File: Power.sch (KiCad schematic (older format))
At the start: 7 parts, among them J7 Screw_Terminal_01x02

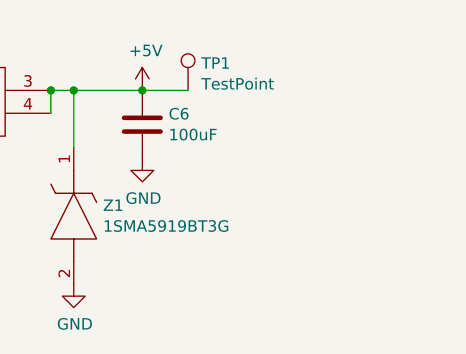
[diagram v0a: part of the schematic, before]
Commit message: Added in Servo Outputs and Setup the timers in CubeMX
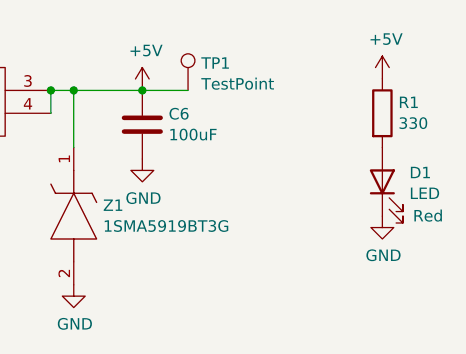
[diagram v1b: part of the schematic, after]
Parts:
- added D1: LED, LED_SMD:LED_0603_1608Metric_Pad1.05x0.95mm_HandSolder, symbol Device:LED
- added R1: 330, Resistor_SMD:R_0603_1608Metric_Pad1.05x0.95mm_HandSolder, symbol Device:R
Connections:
- net +5V: now also R1.1
- net GND: now also D1.1 (K)
- new net: D1.2 (A), R1.2
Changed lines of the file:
@@
 $Descr A4 11693 8268
 encoding utf-8
-Sheet 4 5
+Sheet 4 7
 Title "Power handling"
 Date ""
@@
 Text HLabel 3750 3100 0    50   Input ~ 0
 VDD_5V_Brick
+$Comp
+L Device:LED D?
+U 1 1 5F06186F
+P 7750 3500
+AR Path="/5F06186F" Ref="D?"  Part="1"
+AR Path="/5EF6B0D5/5F06186F" Ref="D1"  Part="1"
+F 0 "D1" V 7789 3382 50  0000 R CNN
+F 1 "LED" V 7698 3382 50  0000 R CNN
+F 2 "LED_SMD:LED_0603_1608Metric_Pad1.05x0.95mm_HandSolder" H 7750 3500 50  0001 C CNN
+F 3 "http://www.farnell.com/datasheets/2186941.pdf" H 7750 3500 50  0001 C CNN
+F 4 "SML-D15UWT86C" V 7750 3500 50  0001 C CNN "PartNumber"
+F 5 "ROHM" V 7750 3500 50  0001 C CNN "Manufacturer"
+F 6 "Red" V 7600 3300 50  0000 C CNN "Colour"
+	1    7750 3500
+	0    -1   -1   0
+$EndComp
+$Comp
+L Device:R R?
+U 1 1 5F061875
+P 7750 3200
+AR Path="/5F061875" Ref="R?"  Part="1"
+AR Path="/5EF6B0D5/5F061875" Ref="R1"  Part="1"
+F 0 "R1" H 7820 3246 50  0000 L CNN
+F 1 "330" H 7820 3155 50  0000 L CNN
+F 2 "Resistor_SMD:R_0603_1608Metric_Pad1.05x0.95mm_HandSolder" V 7680 3200 50  0001 C CNN
+F 3 "~" H 7750 3200 50  0001 C CNN
+	1    7750 3200
+	1    0    0    -1
+$EndComp
+$Comp
+L power:+5V #PWR?
+U 1 1 5F06187B
+P 7750 3050
+AR Path="/5F06187B" Ref="#PWR?"  Part="1"
+AR Path="/5EF6B0D5/5F06187B" Ref="#PWR015"  Part="1"
+F 0 "#PWR015" H 7750 2900 50  0001 C CNN
+F 1 "+5V" H 7765 3223 50  0000 C CNN
+F 2 "" H 7750 3050 50  0001 C CNN
+F 3 "" H 7750 3050 50  0001 C CNN
+	1    7750 3050
+	1    0    0    -1
+$EndComp
+$Comp
+L power:GND #PWR?
+U 1 1 5F061881
+P 7750 3650
+AR Path="/5F061881" Ref="#PWR?"  Part="1"
+AR Path="/5EF6B0D5/5F061881" Ref="#PWR016"  Part="1"
+F 0 "#PWR016" H 7750 3400 50  0001 C CNN
+F 1 "GND" H 7755 3477 50  0000 C CNN
+F 2 "" H 7750 3650 50  0001 C CNN
+F 3 "" H 7750 3650 50  0001 C CNN
+	1    7750 3650
+	1    0    0    -1
+$EndComp
 $EndSCHEMATC

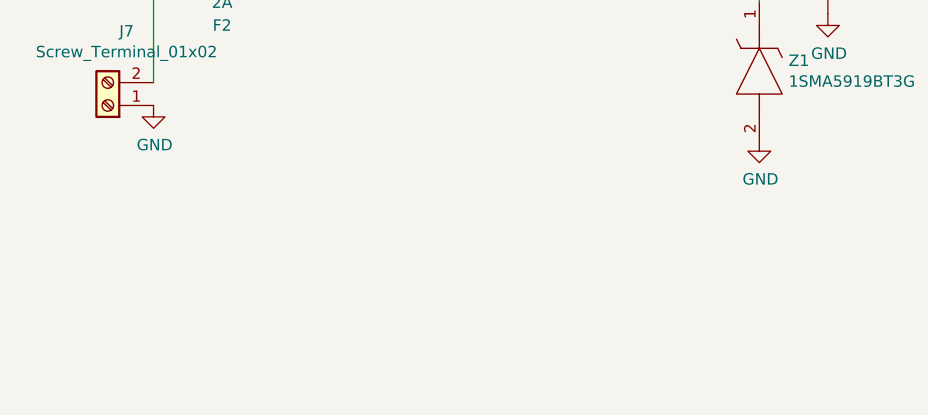
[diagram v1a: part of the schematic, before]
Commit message: Added in Buzzer and N channel mosfet
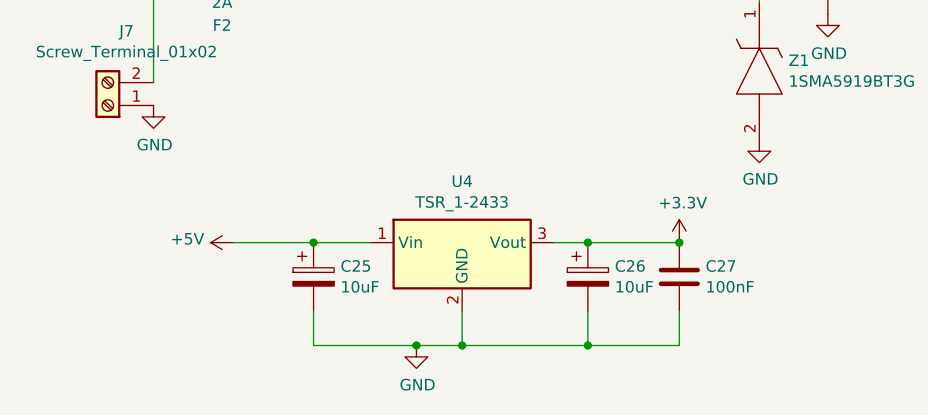
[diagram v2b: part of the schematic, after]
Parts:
- added C25, C26: 10uF, symbol Device:CP
- added C27: 100nF, symbol Device:C
- added U4: TSR_1-2433, Converter_DCDC:Converter_DCDC_TRACO_TSR-1_THT, symbol Regulator_Switching:TSR_1-2433
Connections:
- net +5V: now also C25.1, U4.1 (Vin)
- net GND: now also C25.2, C26.2, C27.2, U4.2 (GND)
- new net +3V3: C26.1, C27.1, U4.3 (Vout)
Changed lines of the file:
@@
 	1    0    0    -1
 $EndComp
+$Comp
+L Regulator_Switching:TSR_1-2433 U4
+U 1 1 5F0F90EB
+P 5100 4500
+F 0 "U4" H 5100 4867 50  0000 C CNN
+F 1 "TSR_1-2433" H 5100 4776 50  0000 C CNN
+F 2 "Converter_DCDC:Converter_DCDC_TRACO_TSR-1_THT" H 5100 4350 50  0001 L CIN
+F 3 "http://www.tracopower.com/products/tsr1.pdf" H 5100 4500 50  0001 C CNN
+	1    5100 4500
+	1    0    0    -1
+$EndComp
+$Comp
+L power:+5V #PWR027
+U 1 1 5F0FA9E4
+P 4100 4400
+F 0 "#PWR027" H 4100 4250 50  0001 C CNN
+F 1 "+5V" V 4115 4528 50  0000 L CNN
+F 2 "" H 4100 4400 50  0001 C CNN
+F 3 "" H 4100 4400 50  0001 C CNN
+	1    4100 4400
+	0    -1   -1   0
+$EndComp
+Wire Wire Line
+	4450 4700 4450 4850
+Wire Wire Line
+	4450 4850 4900 4850
+Wire Wire Line
+	5100 4850 5100 4700
+$Comp
+L power:GND #PWR028
+U 1 1 5F0FC46C
+P 4900 4850
+F 0 "#PWR028" H 4900 4600 50  0001 C CNN
+F 1 "GND" H 4905 4677 50  0000 C CNN
+F 2 "" H 4900 4850 50  0001 C CNN
+F 3 "" H 4900 4850 50  0001 C CNN
+	1    4900 4850
+	1    0    0    -1
+$EndComp
+Connection ~ 4900 4850
+Wire Wire Line
+	4900 4850 5100 4850
+Wire Wire Line
+	5650 4700 5650 4850
+Wire Wire Line
+	5650 4850 5100 4850
+Connection ~ 5100 4850
+$Comp
+L Device:C C27
+U 1 1 5F100D4B
+P 6050 4550
+F 0 "C27" H 6165 4596 50  0000 L CNN
+F 1 "100nF" H 6165 4505 50  0000 L CNN
+F 2 "" H 6088 4400 50  0001 C CNN
+F 3 "~" H 6050 4550 50  0001 C CNN
+	1    6050 4550
+	1    0    0    -1
+$EndComp
+Wire Wire Line
+	6050 4700 6050 4850
+Wire Wire Line
+	6050 4850 5650 4850
+Connection ~ 5650 4850
+Wire Wire Line
+	5500 4400 5650 4400
+$Comp
+L Device:CP C26
+U 1 1 5F102DEA
+P 5650 4550
+F 0 "C26" H 5768 4596 50  0000 L CNN
+F 1 "10uF" H 5768 4505 50  0000 L CNN
+F 2 "" H 5688 4400 50  0001 C CNN
+F 3 "~" H 5650 4550 50  0001 C CNN
+	1    5650 4550
+	1    0    0    -1
+$EndComp
+Connection ~ 5650 4400
+Wire Wire Line
+	5650 4400 6050 4400
+Wire Wire Line
+	4100 4400 4450 4400
+$Comp
+L Device:CP C25
+U 1 1 5F103B0A
+P 4450 4550
+F 0 "C25" H 4568 4596 50  0000 L CNN
+F 1 "10uF" H 4568 4505 50  0000 L CNN
+F 2 "" H 4488 4400 50  0001 C CNN
+F 3 "~" H 4450 4550 50  0001 C CNN
+	1    4450 4550
+	1    0    0    -1
+$EndComp
+Connection ~ 4450 4400
+Wire Wire Line
+	4450 4400 4700 4400
+$Comp
+L power:+3.3V #PWR029
+U 1 1 5F105C55
+P 6050 4400
+F 0 "#PWR029" H 6050 4250 50  0001 C CNN
+F 1 "+3.3V" H 6065 4573 50  0000 C CNN
+F 2 "" H 6050 4400 50  0001 C CNN
+F 3 "" H 6050 4400 50  0001 C CNN
+	1    6050 4400
+	1    0    0    -1
+$EndComp
+Connection ~ 6050 4400
 $EndSCHEMATC

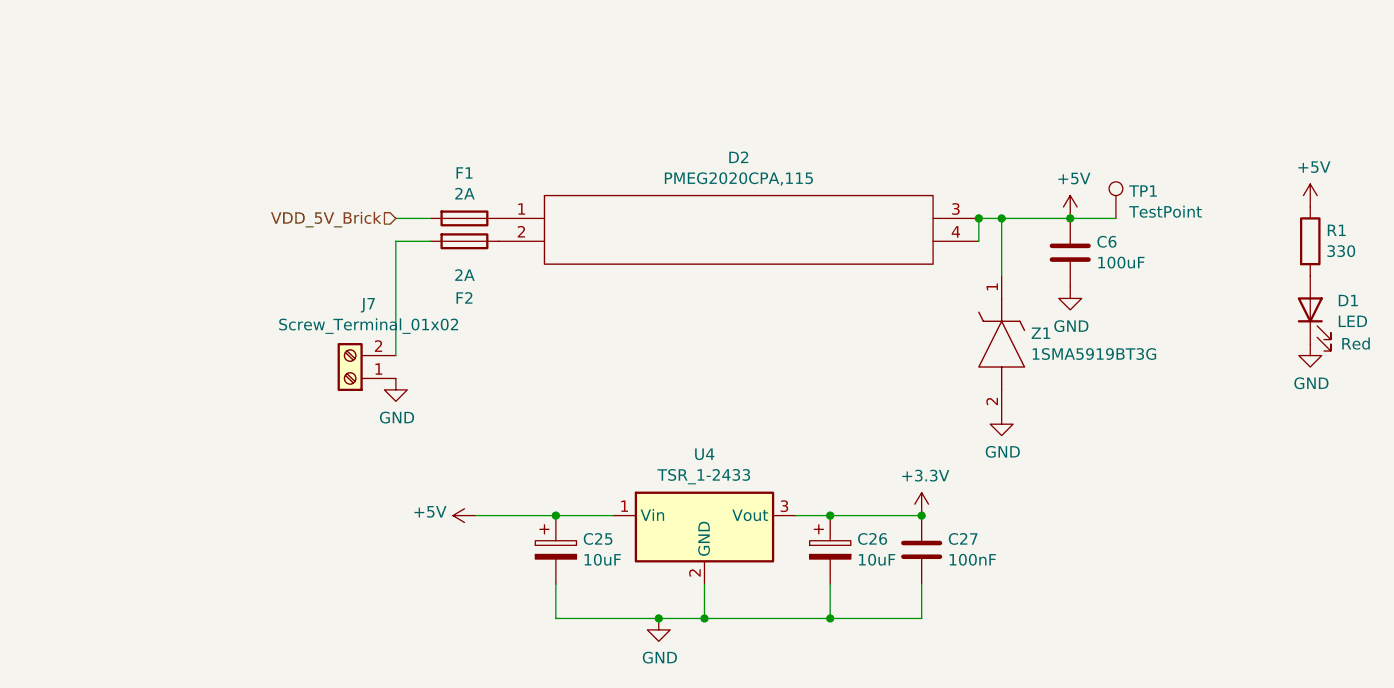
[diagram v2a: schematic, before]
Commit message: IMU1/2 added in plus regs
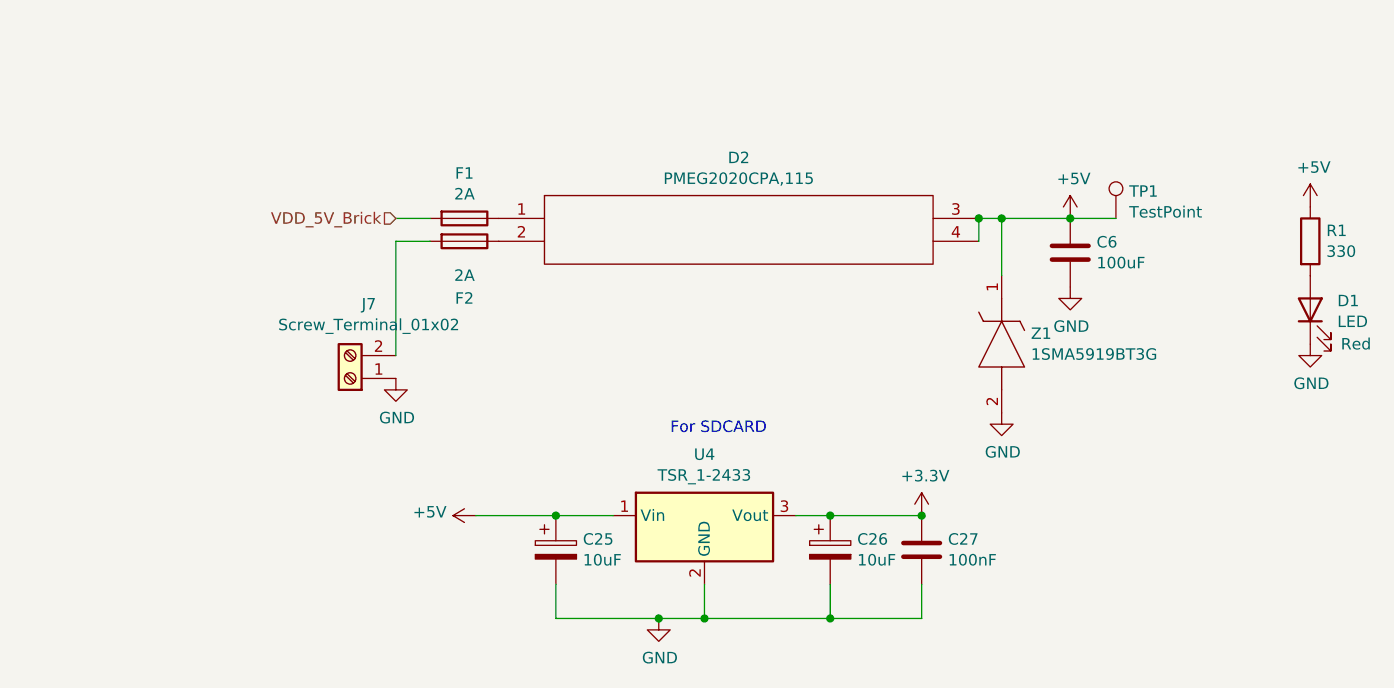
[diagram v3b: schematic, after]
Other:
- note added: "For SDCARD\n"
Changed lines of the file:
@@
 $Descr A4 11693 8268
 encoding utf-8
-Sheet 4 7
+Sheet 4 8
 Title "Power handling"
 Date ""
@@
 $EndComp
 Connection ~ 6050 4400
+Text Notes 4950 4050 0    50   ~ 0
+For SDCARD\n
 $EndSCHEMATC

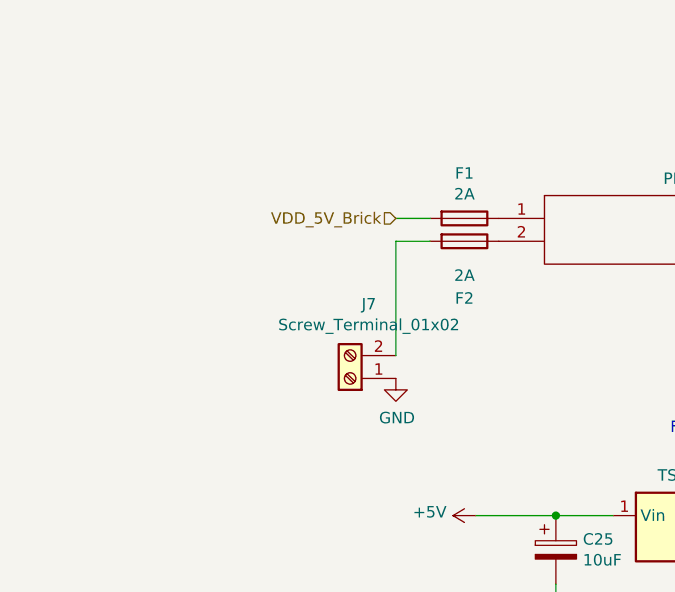
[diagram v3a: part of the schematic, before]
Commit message: Wired up IMUs signals
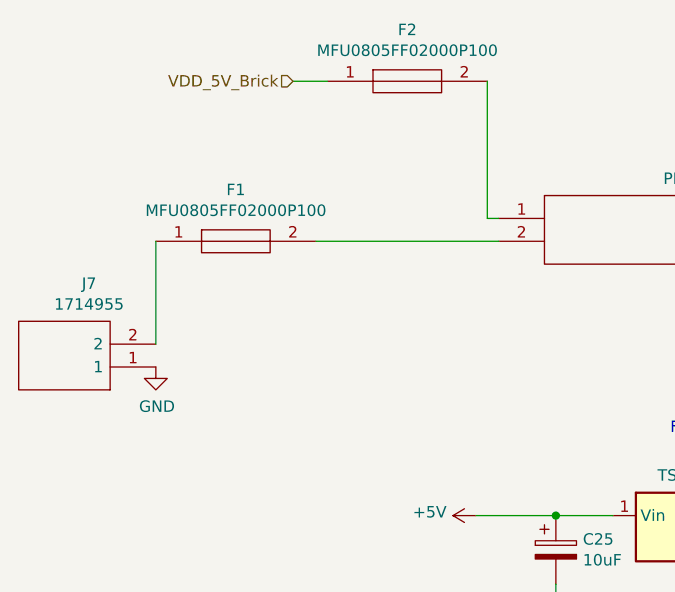
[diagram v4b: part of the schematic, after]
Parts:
- removed F1, F2: 2A, symbol Device:Fuse
- removed J7: Screw_Terminal_01x02, symbol Connector:Screw_Terminal_01x02
- added F1, F2: MFU0805FF02000P100, FUSC2012X55N, symbol SamacSys_Parts:MFU0805FF02000P100
- added J7: 1714955, SHDR2W110P0X635_1X2_1270X1250X2150P, symbol SamacSys_Parts:1714955
- C25: footprint (none) -> Capacitor_SMD:C_0603_1608Metric_Pad1.05x0.95mm_HandSolder; Part No (none) -> GRM188R61A106KE69D
- C26: footprint (none) -> Capacitor_SMD:C_0603_1608Metric_Pad1.05x0.95mm_HandSolder; Part no (none) -> GRM188R61A106KE69D
- C27: footprint (none) -> Capacitor_SMD:C_0603_1608Metric_Pad1.05x0.95mm_HandSolder
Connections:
- net GND: now also J7.1
- net VDD_5V_Brick: now also F2.1
- net at D2.1: now also F2.2
- net at D2.2: now also F1.2
- new net: F1.1, J7.2
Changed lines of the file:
@@
 Wire Wire Line
 	6700 3100 6900 3100
-$Comp
-L Device:Fuse F?
-U 1 1 5EF8875C
-P 4050 3100
-AR Path="/5EF8875C" Ref="F?"  Part="1"
-AR Path="/5EF6B0D5/5EF8875C" Ref="F1"  Part="1"
-F 0 "F1" V 3853 3100 50  0000 C CNN
-F 1 "2A" V 3944 3100 50  0000 C CNN
-F 2 "" V 3980 3100 50  0001 C CNN
-F 3 "~" H 4050 3100 50  0001 C CNN
-	1    4050 3100
-	0    1    1    0
-$EndComp
-Wire Wire Line
-	3750 3100 3900 3100
+Wire Wire Line
+	3300 2500 3450 2500
 $Comp
 L PMEG2020CPA_115:PMEG2020CPA,115 D?
@@
 	1    0    0    -1
 $EndComp
-$Comp
-L Device:Fuse F?
-U 1 1 5EF88772
-P 4050 3200
-AR Path="/5EF88772" Ref="F?"  Part="1"
-AR Path="/5EF6B0D5/5EF88772" Ref="F2"  Part="1"
-F 0 "F2" V 4300 3200 50  0000 C CNN
-F 1 "2A" V 4200 3200 50  0000 C CNN
-F 2 "" V 3980 3200 50  0001 C CNN
-F 3 "~" H 4050 3200 50  0001 C CNN
-	1    4050 3200
-	0    1    1    0
-$EndComp
-$Comp
-L Connector:Screw_Terminal_01x02 J?
-U 1 1 5EF88778
-P 3550 3800
-AR Path="/5EF88778" Ref="J?"  Part="1"
-AR Path="/5EF6B0D5/5EF88778" Ref="J7"  Part="1"
-F 0 "J7" H 3468 3475 50  0000 C CNN
-F 1 "Screw_Terminal_01x02" H 3468 3566 50  0000 C CNN
-F 2 "" H 3550 3800 50  0001 C CNN
-F 3 "~" H 3550 3800 50  0001 C CNN
-	1    3550 3800
-	-1   0    0    1
-$EndComp
-Wire Wire Line
-	3750 3700 3750 3200
-Wire Wire Line
-	3750 3200 3900 3200
+Wire Wire Line
+	2700 3650 2700 3200
 $Comp
 L power:GND #PWR?
 U 1 1 5EF88780
-P 3750 3800
+P 2700 3750
 AR Path="/5EF88780" Ref="#PWR?"  Part="1"
 AR Path="/5EF6B0D5/5EF88780" Ref="#PWR03"  Part="1"
-F 0 "#PWR03" H 3750 3550 50  0001 C CNN
-F 1 "GND" H 3755 3627 50  0000 C CNN
-F 2 "" H 3750 3800 50  0001 C CNN
-F 3 "" H 3750 3800 50  0001 C CNN
-	1    3750 3800
+F 0 "#PWR03" H 2700 3500 50  0001 C CNN
+F 1 "GND" H 2705 3577 50  0000 C CNN
+F 2 "" H 2700 3750 50  0001 C CNN
+F 3 "" H 2700 3750 50  0001 C CNN
+	1    2700 3750
 	1    0    0    -1
 $EndComp
@@
 	1    0    0    -1
 $EndComp
-Text HLabel 3750 3100 0    50   Input ~ 0
+Text HLabel 3300 2500 0    50   Input ~ 0
 VDD_5V_Brick
 $Comp
@@
 F 0 "C27" H 6165 4596 50  0000 L CNN
 F 1 "100nF" H 6165 4505 50  0000 L CNN
-F 2 "" H 6088 4400 50  0001 C CNN
+F 2 "Capacitor_SMD:C_0603_1608Metric_Pad1.05x0.95mm_HandSolder" H 6088 4400 50  0001 C CNN
 F 3 "~" H 6050 4550 50  0001 C CNN
 	1    6050 4550
@@
 F 0 "C26" H 5768 4596 50  0000 L CNN
 F 1 "10uF" H 5768 4505 50  0000 L CNN
-F 2 "" H 5688 4400 50  0001 C CNN
-F 3 "~" H 5650 4550 50  0001 C CNN
+F 2 "Capacitor_SMD:C_0603_1608Metric_Pad1.05x0.95mm_HandSolder" H 5688 4400 50  0001 C CNN
+F 3 "https://search.murata.co.jp/Ceramy/image/img/A01X/G101/ENG/GRM188R61A106KE69-01.pdf" H 5650 4550 50  0001 C CNN
+F 4 "GRM188R61A106KE69D" H 5650 4550 50  0001 C CNN "Part no"
 	1    5650 4550
 	1    0    0    -1
@@
 F 0 "C25" H 4568 4596 50  0000 L CNN
 F 1 "10uF" H 4568 4505 50  0000 L CNN
-F 2 "" H 4488 4400 50  0001 C CNN
-F 3 "~" H 4450 4550 50  0001 C CNN
+F 2 "Capacitor_SMD:C_0603_1608Metric_Pad1.05x0.95mm_HandSolder" H 4488 4400 50  0001 C CNN
+F 3 "https://search.murata.co.jp/Ceramy/image/img/A01X/G101/ENG/GRM188R61A106KE69-01.pdf" H 4450 4550 50  0001 C CNN
+F 4 "GRM188R61A106KE69D" H 4450 4550 50  0001 C CNN "Part No"
 	1    4450 4550
 	1    0    0    -1
@@
 Text Notes 4950 4050 0    50   ~ 0
 For SDCARD\n
+$Comp
+L SamacSys_Parts:1714955 J7
+U 1 1 5ED8CB55
+P 2700 3750
+F 0 "J7" H 2992 3385 50  0000 C CNN
+F 1 "1714955" H 2992 3476 50  0000 C CNN
+F 2 "SHDR2W110P0X635_1X2_1270X1250X2150P" H 3350 3850 50  0001 L CNN
+F 3 "https://www.phoenixcontact.com/online/portal/gb/pxc/product_detail_page/!ut/p/z1/3VdLc9owEP4r5MCtQrKwZdOZHoyZ8moIDknBvngkW6Zq_IoxkPLrKxtoaTqBQ4ZD7NkZS6vdb7VrfxotdOECugndiCUtRJrQSM4dl3gGHluDvqrc9r9aGJn3g9HQviMmwRr8Dl3oFpRBRylHkWA5zX9BZ8l4UioyEcglXVE7mlbO03" H 3350 3750 50  0001 L CNN
+F 4 "PHOENIX CONTACT - 1714955 - TERMINAL BLOCK, WIRE TO BRD, 2POS, 10AWG" H 3350 3650 50  0001 L CNN "Description"
+F 5 "21.5" H 3350 3550 50  0001 L CNN "Height"
+F 6 "Phoenix Contact" H 3350 3450 50  0001 L CNN "Manufacturer_Name"
+F 7 "1714955" H 3350 3350 50  0001 L CNN "Manufacturer_Part_Number"
+F 8 "1714955" H 3350 3250 50  0001 L CNN "Arrow Part Number"
+F 9 "https://www.arrow.com/en/products/1714955/phoenix-contact" H 3350 3150 50  0001 L CNN "Arrow Price/Stock"
+F 10 "651-1714955" H 3350 3050 50  0001 L CNN "Mouser Part Number"
+F 11 "https://www.mouser.co.uk/ProductDetail/Phoenix-Contact/1714955?qs=cyzODkzcbwAF65hL8%2FUyaQ%3D%3D" H 3350 2950 50  0001 L CNN "Mouser Price/Stock"
+	1    2700 3750
+	-1   0    0    1
+$EndComp
+$Comp
+L SamacSys_Parts:MFU0805FF02000P100 F1
+U 1 1 5ED8EA12
+P 2700 3200
+F 0 "F1" H 3050 3425 50  0000 C CNN
+F 1 "MFU0805FF02000P100" H 3050 3334 50  0000 C CNN
+F 2 "FUSC2012X55N" H 3250 3250 50  0001 L CNN
+F 3 "http://www.mouser.com/datasheet/2/427/mfuserie-239895.pdf" H 3250 3150 50  0001 L CNN
+F 4 "VISHAY - MFU0805FF02000P100 - FUSE, 0805 SMD, 2A" H 3250 3050 50  0001 L CNN "Description"
+F 5 "0.55" H 3250 2950 50  0001 L CNN "Height"
+F 6 "Vishay" H 3250 2850 50  0001 L CNN "Manufacturer_Name"
+F 7 "MFU0805FF02000P100" H 3250 2750 50  0001 L CNN "Manufacturer_Part_Number"
+F 8 "MFU0805FF02000P100" H 3250 2650 50  0001 L CNN "Arrow Part Number"
+F 9 "https://www.arrow.com/en/products/mfu0805ff02000p100/vishay" H 3250 2550 50  0001 L CNN "Arrow Price/Stock"
+F 10 "594-MFU0805FF02000P1" H 3250 2450 50  0001 L CNN "Mouser Part Number"
+F 11 "https://www.mouser.co.uk/ProductDetail/Vishay-Beyschlag/MFU0805FF02000P100?qs=oI046glRurtNfIoauhkpAQ%3D%3D" H 3250 2350 50  0001 L CNN "Mouser Price/Stock"
+	1    2700 3200
+	1    0    0    -1
+$EndComp
+Wire Wire Line
+	4200 3200 3400 3200
+$Comp
+L SamacSys_Parts:MFU0805FF02000P100 F2
+U 1 1 5ED92F76
+P 3450 2500
+F 0 "F2" H 3800 2725 50  0000 C CNN
+F 1 "MFU0805FF02000P100" H 3800 2634 50  0000 C CNN
+F 2 "FUSC2012X55N" H 4000 2550 50  0001 L CNN
+F 3 "http://www.mouser.com/datasheet/2/427/mfuserie-239895.pdf" H 4000 2450 50  0001 L CNN
+F 4 "VISHAY - MFU0805FF02000P100 - FUSE, 0805 SMD, 2A" H 4000 2350 50  0001 L CNN "Description"
+F 5 "0.55" H 4000 2250 50  0001 L CNN "Height"
+F 6 "Vishay" H 4000 2150 50  0001 L CNN "Manufacturer_Name"
+F 7 "MFU0805FF02000P100" H 4000 2050 50  0001 L CNN "Manufacturer_Part_Number"
+F 8 "MFU0805FF02000P100" H 4000 1950 50  0001 L CNN "Arrow Part Number"
+F 9 "https://www.arrow.com/en/products/mfu0805ff02000p100/vishay" H 4000 1850 50  0001 L CNN "Arrow Price/Stock"
+F 10 "594-MFU0805FF02000P1" H 4000 1750 50  0001 L CNN "Mouser Part Number"
+F 11 "https://www.mouser.co.uk/ProductDetail/Vishay-Beyschlag/MFU0805FF02000P100?qs=oI046glRurtNfIoauhkpAQ%3D%3D" H 4000 1650 50  0001 L CNN "Mouser Price/Stock"
+	1    3450 2500
+	1    0    0    -1
+$EndComp
+Wire Wire Line
+	4150 2500 4150 3100
+Wire Wire Line
+	4150 3100 4200 3100
 $EndSCHEMATC
